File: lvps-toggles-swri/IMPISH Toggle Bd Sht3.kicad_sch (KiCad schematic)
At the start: 66 parts, among them J3 BCS-110-L-D-TE, J4 BCS-110-L-D-TE, Q1 MMBT3904Q, Q10 MMBT3904Q, Q11 MMBT3906Q, Q12 ZXM61N02F, Q2 MMBT3906Q, Q3 ZXM61N02F, Q4 MMBT3904Q, Q5 MMBT3906Q, Q6 ZXM61N02F, Q7 MMBT3904Q, Q8 MMBT3906Q, Q9 ZXM61N02F, U1 BSP452, U2 AP22804AW5-7, U3 AP22804AW5-7, U4 BSP452, U5 AP22804AW5-7, U6 AP22804AW5-7

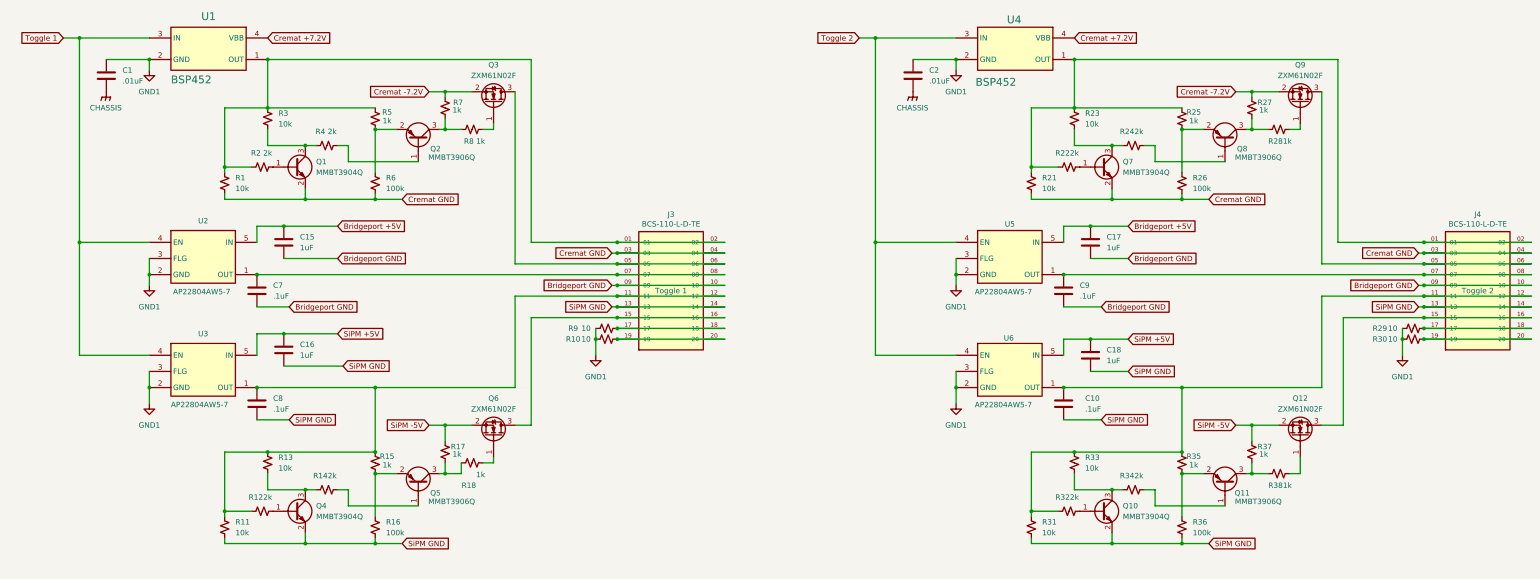
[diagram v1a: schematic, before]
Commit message: swri toggles: start one ground
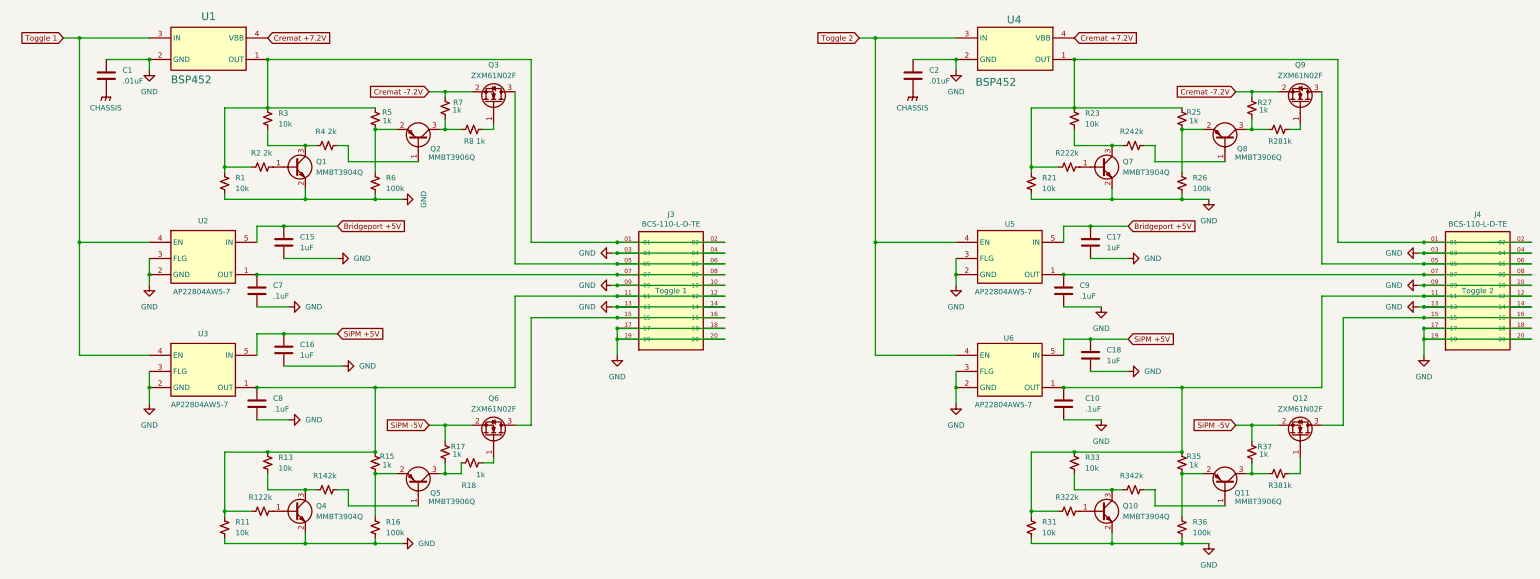
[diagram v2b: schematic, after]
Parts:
- removed R10, R29, R30, R9: 10, Resistor_SMD:R_0805_2012Metric_Pad1.20x1.40mm_HandSolder, symbol Device:R_Small_US
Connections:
- net Bridgeport GND is gone; now on net GND: C15.2, C17.2, C7.2, C9.2, J3.09, J3.10, J4.09, J4.10
- net Cremat GND is gone; now on net GND: J3.03, J3.04, J4.03, J4.04, Q1.2 (E), Q7.2 (E), R1.2, R21.2, R26.2, R6.2
- net GND1 is gone; now on net GND: C1.1, C2.2, U1.2 (GND), U2.2 (GND), U2.3 (FLG), U3.2 (GND), U3.3 (FLG), U4.2 (GND), U5.2 (GND), U5.3 (FLG), U6.2 (GND), U6.3 (FLG)
- net SiPM GND is gone; now on net GND: C10.2, C16.2, C18.2, C8.2, J3.13, J3.14, J4.13, J4.14, Q10.2 (E), Q4.2 (E), R11.2, R16.2, R31.2, R36.2
- net GND: now reaches J4.17, J4.18
- net GND: now also J3.17, J3.18, J3.19, J3.20, J4.19, J4.20
